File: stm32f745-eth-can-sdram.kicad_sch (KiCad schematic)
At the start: 0 parts

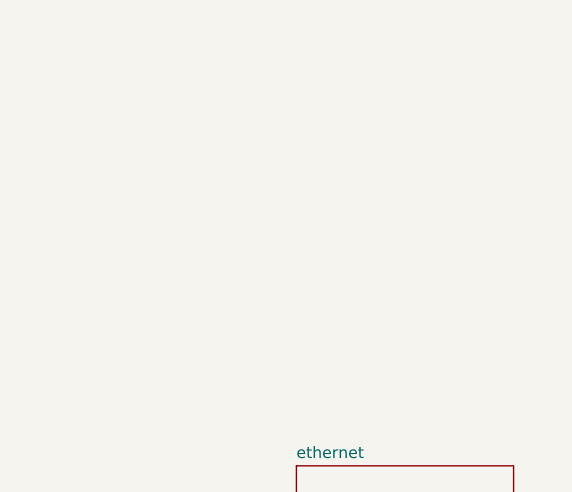
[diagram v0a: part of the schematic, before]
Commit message: add POE schematics, Ethernet phy
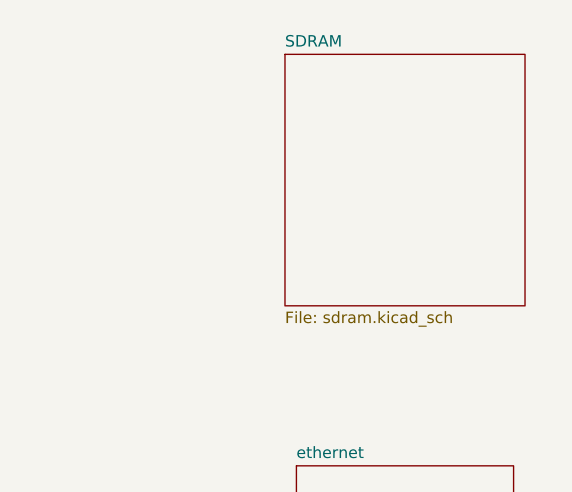
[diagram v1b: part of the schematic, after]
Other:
- added sheet SDRAM (sdram.kicad_sch)
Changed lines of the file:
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@@
+    )
+  )
+  (sheet (at 106.68 123.19) (size 26.67 27.94) (fields_autoplaced)
+    (stroke (width 0.1524) (type solid))
+    (fill (color 0 0 0 0.0000))
+    (property "Sheetname" "SDRAM" (at 106.68 122.4784 0)
+      (effects (font (size 1.27 1.27)) (justify left bottom))
+    )
+    (property "Sheetfile" "sdram.kicad_sch" (at 106.68 151.7146 0)
+      (effects (font (size 1.27 1.27)) (justify left top))
+    )
+    (instances
+      (project "stm32f745-eth-can-sdram"
+        (path "/2fe210a3-bd39-4a0d-882e-a71d33b1f0de" (page "7"))
+      )
     )
   )
